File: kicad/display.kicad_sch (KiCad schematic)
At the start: 205 parts

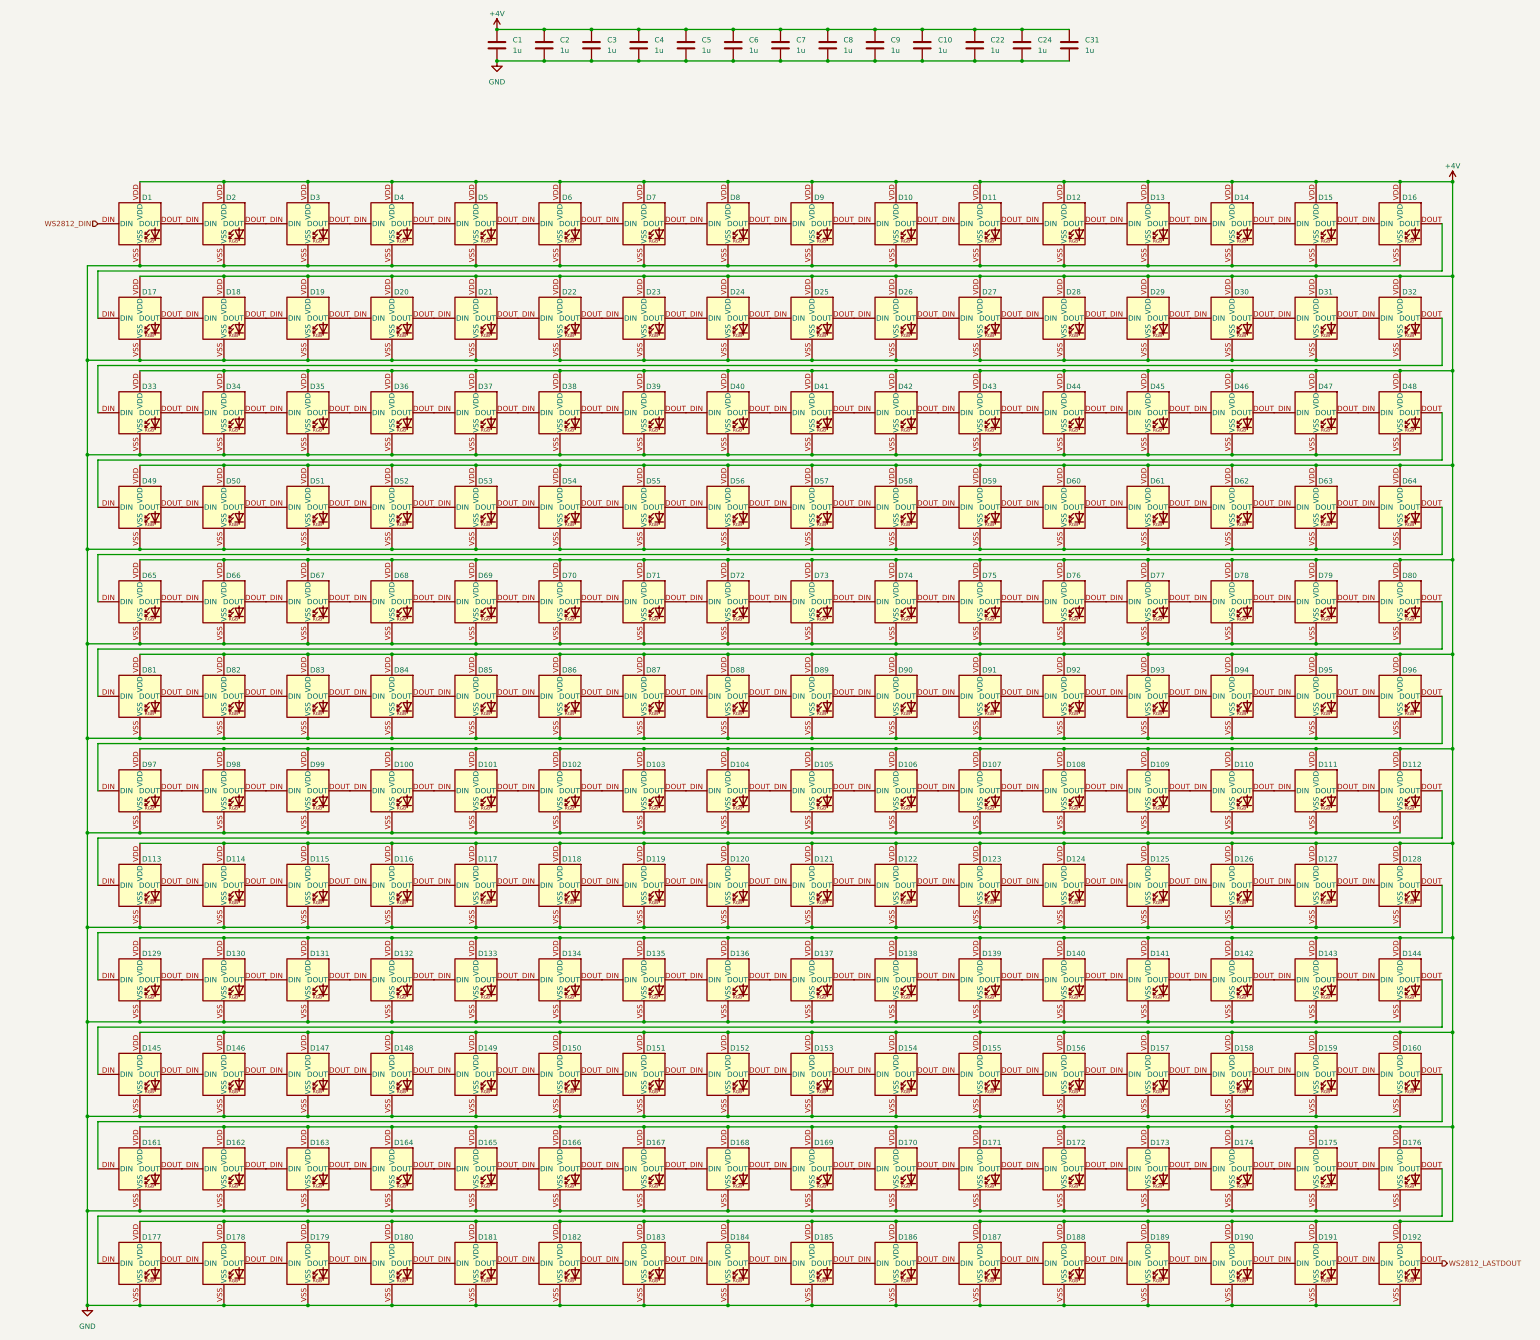
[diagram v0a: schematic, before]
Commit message: fixed all rev0 issues
connected buzzer and bootsel nets
changed IMU to I2C mode
changed IMU to the cheaper -C model
changed all buttons to PTS815
changed order of WS2812s so that the frame buffer can be shifted monolithically
changed boost converter feedback network to use JLCPCB basic parts
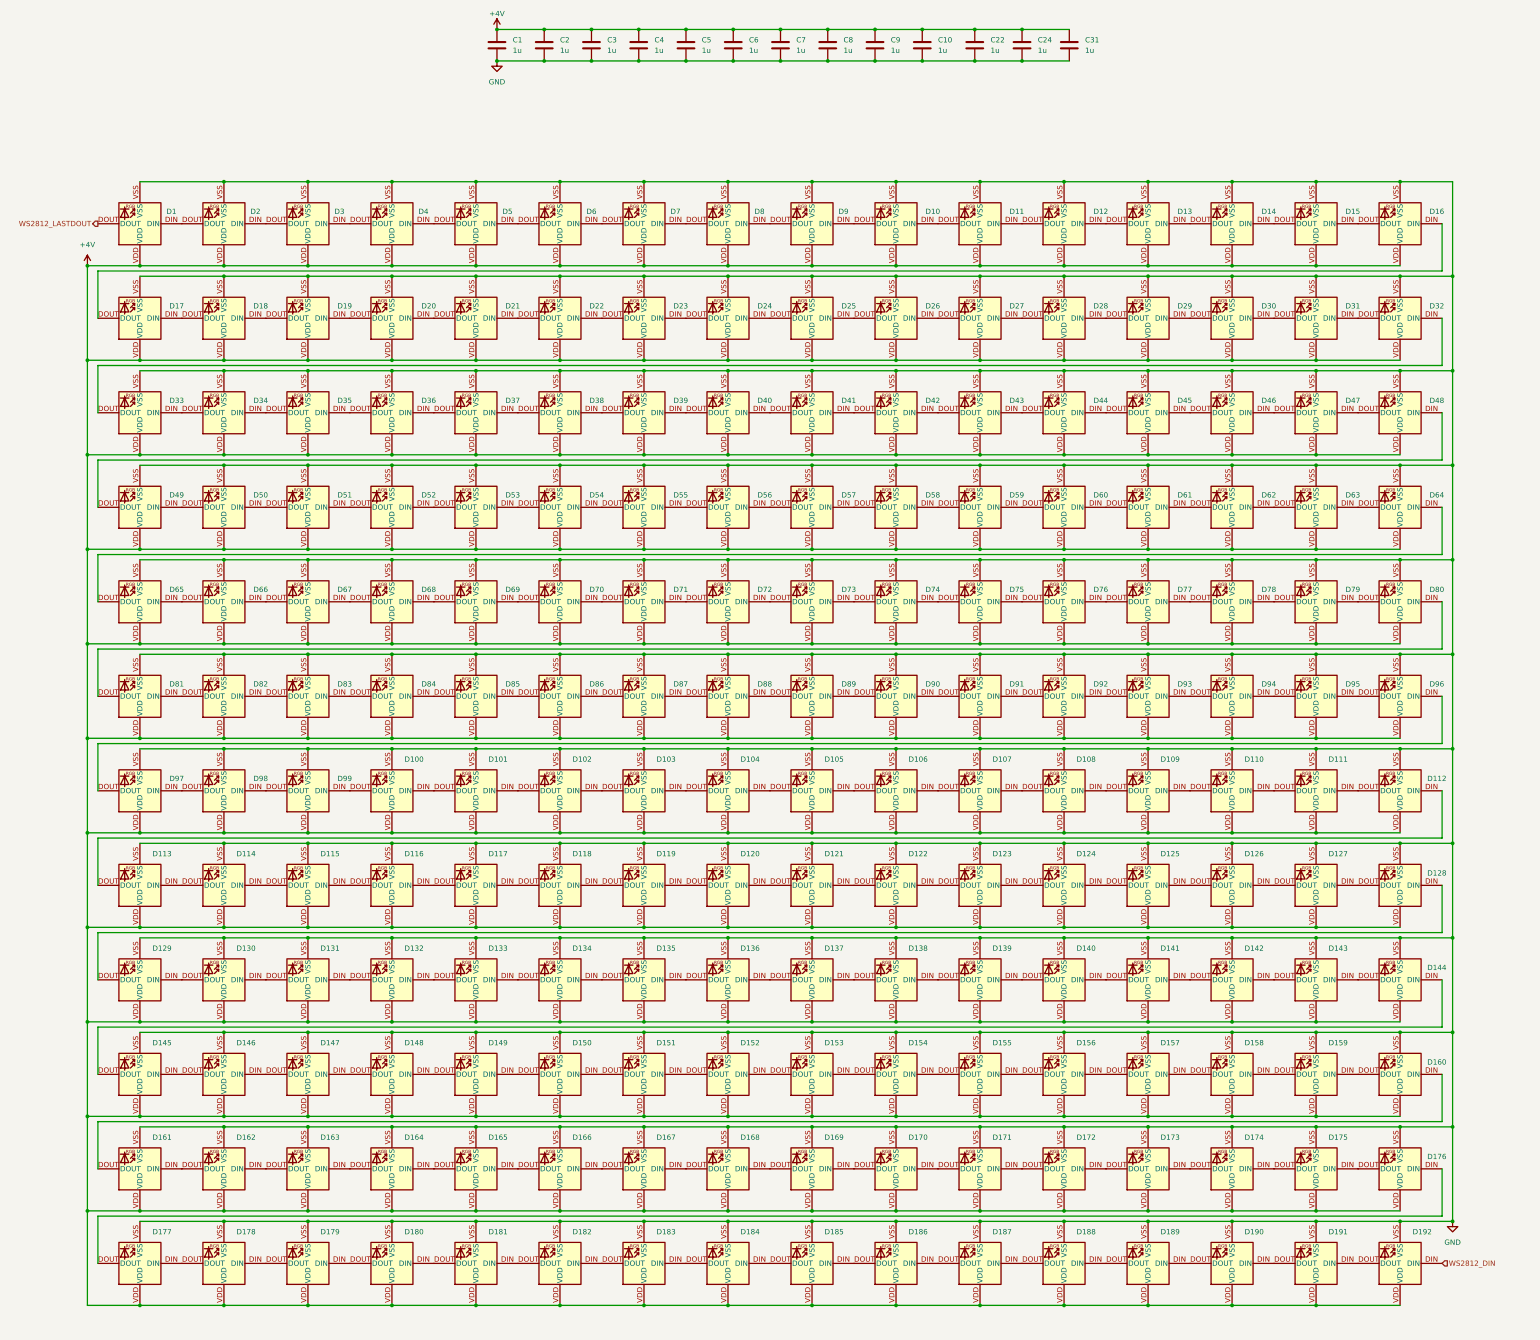
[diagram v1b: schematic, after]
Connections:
- net WS2812_DIN: now also D192.DIN; no longer D1.DIN
- net WS2812_LASTDOUT: now also D1.DOUT; no longer D192.DOUT
- net at D94.DIN: now also D95.DOUT; no longer D93.DOUT
- net at D94.DOUT: now also D93.DIN; no longer D95.DIN
- net at D69.DIN: now also D70.DOUT; no longer D68.DOUT
- net at D69.DOUT: now also D68.DIN; no longer D70.DIN
- net at D139.DIN: now also D140.DOUT; no longer D138.DOUT
- net at D139.DOUT: now also D138.DIN; no longer D140.DIN
- net at D91.DIN: now also D92.DOUT; no longer D90.DOUT
- net at D91.DOUT: now also D90.DIN; no longer D92.DIN
- net at D40.DIN: now also D41.DOUT; no longer D39.DOUT
- net at D40.DOUT: now also D39.DIN; no longer D41.DIN
- net at D104.DIN: now also D105.DOUT; no longer D103.DOUT
- net at D104.DOUT: now also D103.DIN; no longer D105.DIN
- net at D180.DIN: now also D181.DOUT; no longer D179.DOUT
- net at D180.DOUT: now also D179.DIN; no longer D181.DIN
- net at D122.DIN: now also D123.DOUT; no longer D121.DOUT
- net at D122.DOUT: now also D121.DIN; no longer D123.DIN
- net at D20.DIN: now also D21.DOUT; no longer D19.DOUT
- net at D20.DOUT: now also D19.DIN; no longer D21.DIN
- net at D2.DIN: now also D3.DOUT; no longer D1.DOUT
- net at D53.DIN: now also D54.DOUT; no longer D52.DOUT
- net at D53.DOUT: now also D52.DIN; no longer D54.DIN
- net at D81.DIN: now also D82.DOUT; no longer D80.DOUT
- net at D81.DOUT: now also D80.DIN; no longer D82.DIN
- net at D127.DIN: now also D128.DOUT; no longer D126.DOUT
- net at D127.DOUT: now also D126.DIN; no longer D128.DIN
- net at D79.DIN: now also D80.DOUT; no longer D78.DOUT
- net at D79.DOUT: now also D78.DIN; no longer D80.DIN
- net at D149.DIN: now also D150.DOUT; no longer D148.DOUT
- net at D149.DOUT: now also D148.DIN; no longer D150.DIN
- net at D64.DIN: now also D65.DOUT; no longer D63.DOUT
- net at D64.DOUT: now also D63.DIN; no longer D65.DIN
- net at D131.DIN: now also D132.DOUT; no longer D130.DOUT
- net at D131.DOUT: now also D130.DIN; no longer D132.DIN
- net at D133.DIN: now also D134.DOUT; no longer D132.DOUT
- net at D133.DOUT: now also D132.DIN; no longer D134.DIN
- net at D106.DIN: now also D107.DOUT; no longer D105.DOUT
- net at D106.DOUT: now also D105.DIN; no longer D107.DIN
- net at D172.DIN: now also D173.DOUT; no longer D171.DOUT
- net at D172.DOUT: now also D171.DIN; no longer D173.DIN
- net at D57.DIN: now also D58.DOUT; no longer D56.DOUT
- net at D57.DOUT: now also D56.DIN; no longer D58.DIN
- net at D66.DIN: now also D67.DOUT; no longer D65.DOUT
- net at D66.DOUT: now also D65.DIN; no longer D67.DIN
- net at D13.DIN: now also D14.DOUT; no longer D12.DOUT
- net at D13.DOUT: now also D12.DIN; no longer D14.DIN
- net at D61.DIN: now also D62.DOUT; no longer D60.DOUT
- net at D61.DOUT: now also D60.DIN; no longer D62.DIN
- net at D38.DOUT: now also D37.DIN; no longer D39.DIN
- net at D73.DIN: now also D74.DOUT; no longer D72.DOUT
- net at D73.DOUT: now also D72.DIN; no longer D74.DIN
- net at D18.DIN: now also D19.DOUT; no longer D17.DOUT
- net at D18.DOUT: now also D17.DIN; no longer D19.DIN
- net at D166.DIN: now also D167.DOUT; no longer D165.DOUT
- net at D166.DOUT: now also D165.DIN; no longer D167.DIN
- net at D51.DIN: now also D52.DOUT; no longer D50.DOUT
- net at D51.DOUT: now also D50.DIN; no longer D52.DIN
- net at D22.DIN: now also D23.DOUT; no longer D21.DOUT
- net at D22.DOUT: now also D21.DIN; no longer D23.DIN
- net at D38.DIN: now also D39.DOUT; no longer D37.DOUT
- net at D24.DIN: now also D25.DOUT; no longer D23.DOUT
- net at D24.DOUT: now also D23.DIN; no longer D25.DIN
- net at D164.DIN: now also D165.DOUT; no longer D163.DOUT
- net at D164.DOUT: now also D163.DIN; no longer D165.DIN
- net at D174.DIN: now also D175.DOUT; no longer D173.DOUT
- net at D170.DIN: now also D171.DOUT; no longer D169.DOUT
- net at D170.DOUT: now also D169.DIN; no longer D171.DIN
- net at D119.DIN: now also D120.DOUT; no longer D118.DOUT
- net at D119.DOUT: now also D118.DIN; no longer D120.DIN
- net at D77.DIN: now also D78.DOUT; no longer D76.DOUT
- net at D77.DOUT: now also D76.DIN; no longer D78.DIN
- net at D153.DIN: now also D154.DOUT; no longer D152.DOUT
- net at D153.DOUT: now also D152.DIN; no longer D154.DIN
- net at D75.DIN: now also D76.DOUT; no longer D74.DOUT
- net at D113.DIN: now also D114.DOUT; no longer D112.DOUT
- net at D113.DOUT: now also D112.DIN; no longer D114.DIN
- net at D190.DIN: now also D191.DOUT; no longer D189.DOUT
- net at D190.DOUT: now also D189.DIN; no longer D191.DIN
- net at D42.DIN: now also D43.DOUT; no longer D41.DOUT
- net at D46.DIN: now also D47.DOUT; no longer D45.DOUT
- net at D46.DOUT: now also D45.DIN; no longer D47.DIN
- net at D109.DIN: now also D110.DOUT; no longer D108.DOUT
- net at D109.DOUT: now also D108.DIN; no longer D110.DIN
- net at D89.DIN: now also D90.DOUT; no longer D88.DOUT
- net at D89.DOUT: now also D88.DIN; no longer D90.DIN
- net at D33.DIN: now also D34.DOUT; no longer D32.DOUT
- net at D33.DOUT: now also D32.DIN; no longer D34.DIN
- net at D157.DIN: now also D158.DOUT; no longer D156.DOUT
- net at D157.DOUT: now also D156.DIN; no longer D158.DIN
- net at D59.DIN: now also D60.DOUT; no longer D58.DOUT
- net at D59.DOUT: now also D58.DIN; no longer D60.DIN
- net at D48.DIN: now also D49.DOUT; no longer D47.DOUT
- net at D115.DIN: now also D116.DOUT; no longer D114.DOUT
- net at D115.DOUT: now also D114.DIN; no longer D116.DIN
- net at D129.DOUT: now also D128.DIN; no longer D130.DIN
- net at D117.DIN: now also D118.DOUT; no longer D116.DOUT
- net at D129.DIN: now also D130.DOUT; no longer D128.DOUT
- net at D188.DIN: now also D189.DOUT; no longer D187.DOUT
- net at D188.DOUT: now also D187.DIN; no longer D189.DIN
- net at D124.DIN: now also D125.DOUT; no longer D123.DOUT
- net at D124.DOUT: now also D123.DIN; no longer D125.DIN
- net at D135.DIN: now also D136.DOUT; no longer D134.DOUT
- net at D4.DIN: now also D5.DOUT; no longer D3.DOUT
- net at D4.DOUT: now also D3.DIN; no longer D5.DIN
- net at D11.DIN: now also D12.DOUT; no longer D10.DOUT
- net at D11.DOUT: now also D10.DIN; no longer D12.DIN
- net at D2.DOUT: now also D1.DIN; no longer D3.DIN
- net at D111.DIN: now also D112.DOUT; no longer D110.DOUT
- net at D96.DIN: now also D97.DOUT; no longer D95.DOUT
- net at D96.DOUT: now also D95.DIN; no longer D97.DIN
- net at D99.DIN: now also D100.DOUT; no longer D98.DOUT
- net at D99.DOUT: now also D98.DIN; no longer D100.DIN
- net at D8.DIN: now also D9.DOUT; no longer D7.DOUT
- net at D8.DOUT: now also D7.DIN; no longer D9.DIN
- net at D182.DIN: now also D183.DOUT; no longer D181.DOUT
- net at D147.DIN: now also D148.DOUT; no longer D146.DOUT
- net at D147.DOUT: now also D146.DIN; no longer D148.DIN
- net at D160.DIN: now also D161.DOUT; no longer D159.DOUT
- net at D160.DOUT: now also D159.DIN; no longer D161.DIN
- net at D55.DIN: now also D56.DOUT; no longer D54.DOUT
- net at D186.DIN: now also D187.DOUT; no longer D185.DOUT
- net at D186.DOUT: now also D185.DIN; no longer D187.DIN
- net at D15.DIN: now also D16.DOUT; no longer D14.DOUT
- net at D15.DOUT: now also D14.DIN; no longer D16.DIN
- net at D182.DOUT: now also D181.DIN; no longer D183.DIN
- net at D75.DOUT: now also D74.DIN; no longer D76.DIN
- net at D168.DIN: now also D169.DOUT; no longer D167.DOUT
- net at D168.DOUT: now also D167.DIN; no longer D169.DIN
- net at D71.DOUT: now also D70.DIN; no longer D72.DIN
- net at D71.DIN: now also D72.DOUT; no longer D70.DOUT
- net at D83.DIN: now also D84.DOUT; no longer D82.DOUT
- net at D83.DOUT: now also D82.DIN; no longer D84.DIN
- net at D87.DIN: now also D88.DOUT; no longer D86.DOUT
- net at D87.DOUT: now also D86.DIN; no longer D88.DIN
- net at D178.DOUT: now also D177.DIN; no longer D179.DIN
- net at D35.DIN: now also D36.DOUT; no longer D34.DOUT
- net at D31.DIN: now also D32.DOUT; no longer D30.DOUT
- net at D31.DOUT: now also D30.DIN; no longer D32.DIN
- net at D144.DIN: now also D145.DOUT; no longer D143.DOUT
- net at D144.DOUT: now also D143.DIN; no longer D145.DIN
- net at D162.DOUT: now also D161.DIN; no longer D163.DIN
- net at D111.DOUT: now also D110.DIN; no longer D112.DIN
- net at D102.DIN: now also D103.DOUT; no longer D101.DOUT
- net at D102.DOUT: now also D101.DIN; no longer D103.DIN
- net at D28.DIN: now also D29.DOUT; no longer D27.DOUT
- net at D28.DOUT: now also D27.DIN; no longer D29.DIN
- net at D35.DOUT: now also D34.DIN; no longer D36.DIN
- net at D117.DOUT: now also D116.DIN; no longer D118.DIN
- net at D44.DIN: now also D45.DOUT; no longer D43.DOUT
- net at D44.DOUT: now also D43.DIN; no longer D45.DIN
- net at D162.DIN: now also D163.DOUT; no longer D161.DOUT
- net at D174.DOUT: now also D173.DIN; no longer D175.DIN
- net at D6.DIN: now also D7.DOUT; no longer D5.DOUT
- net at D26.DOUT: now also D25.DIN; no longer D27.DIN
- net at D55.DOUT: now also D54.DIN; no longer D56.DIN
- net at D48.DOUT: now also D47.DIN; no longer D49.DIN
- net at D176.DIN: now also D177.DOUT; no longer D175.DOUT
- net at D135.DOUT: now also D134.DIN; no longer D136.DIN
- net at D137.DIN: now also D138.DOUT; no longer D136.DOUT
- net at D151.DIN: now also D152.DOUT; no longer D150.DOUT
- net at D85.DOUT: now also D84.DIN; no longer D86.DIN
- net at D137.DOUT: now also D136.DIN; no longer D138.DIN
- net at D155.DIN: now also D156.DOUT; no longer D154.DOUT
- net at D155.DOUT: now also D154.DIN; no longer D156.DIN
- net at D151.DOUT: now also D150.DIN; no longer D152.DIN
- net at D142.DOUT: now also D141.DIN; no longer D143.DIN
- net at D176.DOUT: now also D175.DIN; no longer D177.DIN
- net at D178.DIN: now also D179.DOUT; no longer D177.DOUT
- net at D26.DIN: now also D27.DOUT; no longer D25.DOUT
- net at D142.DIN: now also D143.DOUT; no longer D141.DOUT
- net at D184.DIN: now also D185.DOUT; no longer D183.DOUT
- net at D184.DOUT: now also D183.DIN; no longer D185.DIN
- net at D85.DIN: now also D86.DOUT; no longer D84.DOUT
- net at D42.DOUT: now also D41.DIN; no longer D43.DIN
- net at D6.DOUT: now also D5.DIN; no longer D7.DIN
- new net: D92.DIN, D93.DOUT
- new net: D67.DIN, D68.DOUT
- new net: D125.DIN, D126.DOUT
- new net: D191.DIN, D192.DOUT
- new net: D97.DIN, D98.DOUT
- new net: D107.DIN, D108.DOUT
- new net: D49.DIN, D50.DOUT
- new net: D158.DIN, D159.DOUT
- new net: D145.DIN, D146.DOUT
- new net: D10.DOUT, D9.DIN
- new net: D16.DIN, D17.DOUT
- new net: D36.DIN, D37.DOUT
- new net: D29.DIN, D30.DOUT
- new net: D100.DIN, D101.DOUT
- new net: D120.DIN, D121.DOUT
- new net: D140.DIN, D141.DOUT
- new net: D62.DIN, D63.DOUT
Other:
- title: (none) -> SuperXBit192 WS2812 Display
- moved on the sheet: D1, D10, D100, D101, D102, D103, D104, D105, D106, D107, D108, D109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
